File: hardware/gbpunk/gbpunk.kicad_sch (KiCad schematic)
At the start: 59 parts, among them J1 CART, J2 SWD_CONNECTOR, J4 SWD_CONNECTOR, P1 USB_C_CONNECTOR, SW7 RESET, SW9 USB_BOOT, U1 RP2040, U2 SN74LVC4245A, U3 W25Q128JVS, U4 NCP1117-3.3_SOT223, U5 SN74LVC4245A, U6 SN74LVC4245A, U7 SN74LVC4245A, Y1 12MHz

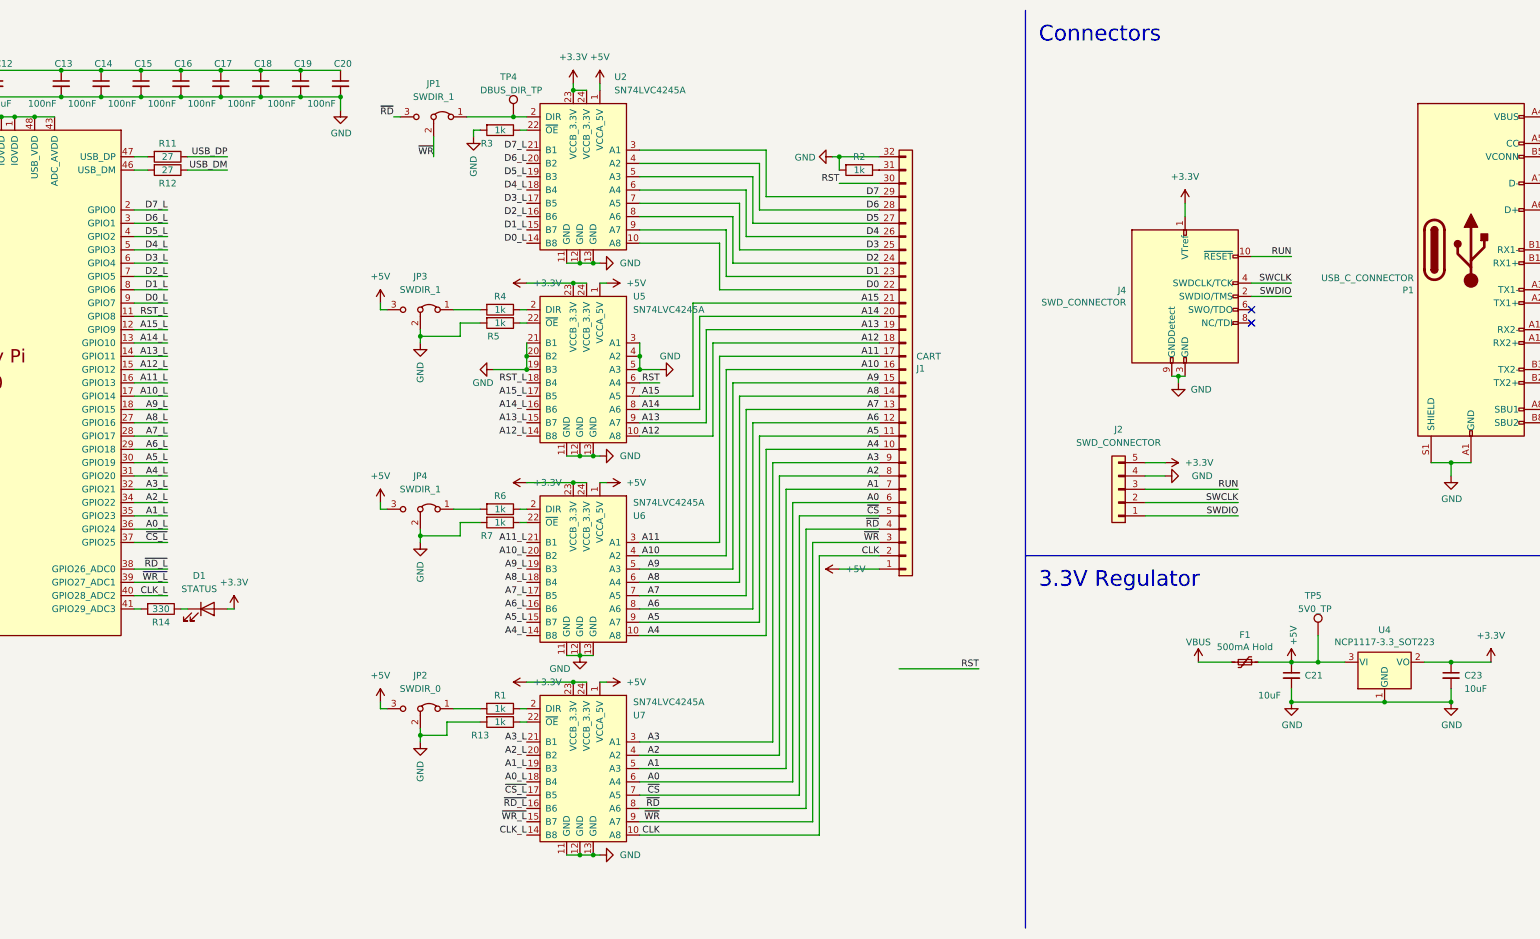
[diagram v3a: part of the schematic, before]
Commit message: added detection circuit and voltage switching for GBA/GB
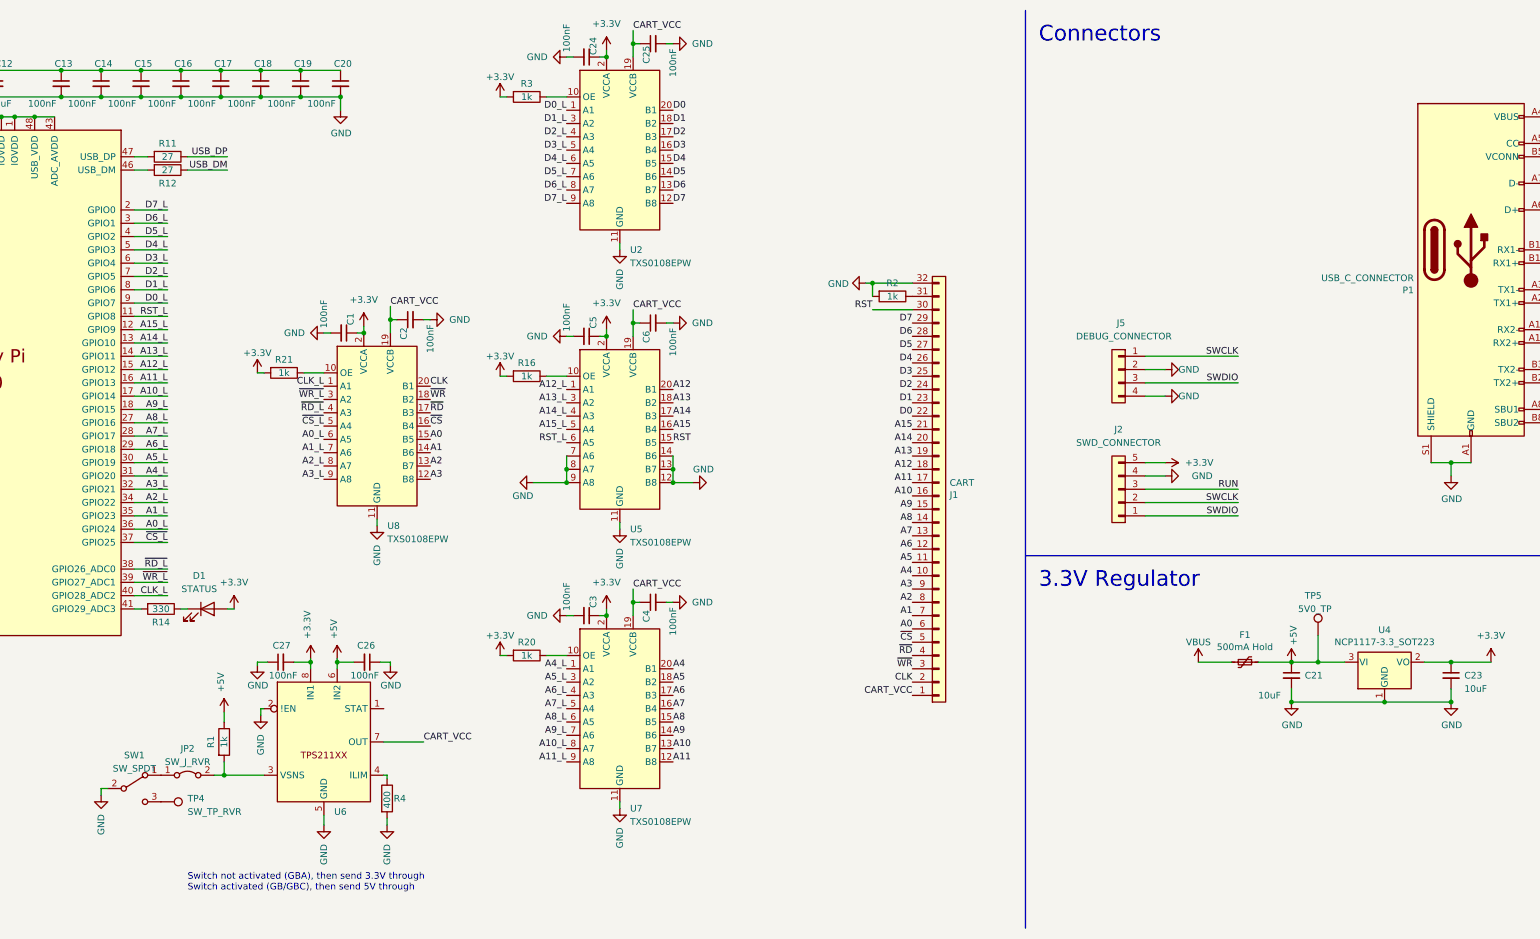
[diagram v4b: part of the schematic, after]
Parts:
- removed J4: SWD_CONNECTOR, Connector_PinHeader_1.27mm:PinHeader_2x05_P1.27mm_Vertical_SMD, symbol Connector:Conn_ARM_JTAG_SWD_10
- removed JP1, JP3, JP4: SWDIR_1, Jumper:SolderJumper-3_P1.3mm_Bridged12_RoundedPad1.0x1.5mm, symbol Jumper:Jumper_3_Bridged12
- removed JP2: SWDIR_0, Jumper:SolderJumper-3_P1.3mm_Bridged12_RoundedPad1.0x1.5mm, symbol Jumper:Jumper_3_Bridged12
- removed R13, R5, R6, R7: 1k, Resistor_SMD:R_0603_1608Metric_Pad0.98x0.95mm_HandSolder, symbol Device:R
- removed U2, U5, U6, U7: SN74LVC4245A, Package_SO:TSSOP-24_4.4x7.8mm_P0.65mm, symbol gbpunk:SN74LVC4245A
- added C1, C2, C24, C25, C26, C27, C3, C4, C5, C6: 100nF, Capacitor_SMD:C_0402_1005Metric_Pad0.74x0.62mm_HandSolder, symbol Device:C_Small
- added J5: DEBUG_CONNECTOR, Connector_JST:JST_GH_SM03B-GHS-TB_1x03-1MP_P1.25mm_Horizontal, symbol Connector_Generic:Conn_01x04
- added JP2: SW_J_RVR, symbol Jumper:Jumper_2_Bridged
- added R16, R20, R21: 1k, Resistor_SMD:R_0603_1608Metric_Pad0.98x0.95mm_HandSolder, symbol Device:R
- added SW1: SW_SPDT, symbol Switch:SW_SPDT
- added U2, U5, U7, U8: TXS0108EPW, Package_SO:TSSOP-20_4.4x6.5mm_P0.65mm, symbol Logic_LevelTranslator:TXS0108EPW
- added U6: ~, symbol gbpunk:TPS211XX
- R4: value 1k -> 400; footprint Resistor_SMD:R_0603_1608Metric_Pad0.98x0.95mm_HandSolder -> (none)
- TP4: value DBUS_DIR_TP -> SW_TP_RVR; footprint TestPoint:TestPoint_Pad_D1.0mm -> (none)
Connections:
- net +3.3V: now also R3.2, C1.1, C24.1, C27.2, C3.1, C5.1, R16.2, R20.2, R21.2, U2.2 (VCCA), U5.2 (VCCA), U6.8 (IN1), U7.2 (VCCA), U8.2 (VCCA)
- net +5V: now also R1.1, C26.2, U6.6 (IN2); no longer J1.1 (Pin_1)
- net A0: now also U8.15 (B5)
- net A0_L: now also U8.6 (A5)
- net A1: now also U8.14 (B6)
- net A10: now also U7.13 (B7)
- net A10_L: now also U7.8 (A7)
- net A11: now also U7.12 (B8)
- net A11_L: now also U7.9 (A8)
- net A12: now also U5.20 (B1)
- net A12_L: now also U5.1 (A1)
- net A13: now also U5.18 (B2)
- net A13_L: now also U5.3 (A2)
- net A14: now also U5.17 (B3)
- net A14_L: now also U5.4 (A3)
- net A15: now also U5.16 (B4)
- net A15_L: now also U5.5 (A4)
- net A1_L: now also U8.7 (A6)
- net A2: now also U8.13 (B7)
- net A2_L: now also U8.8 (A7)
- net A3: now also U8.12 (B8)
- net A3_L: now also U8.9 (A8)
- net A4: now also U7.20 (B1)
- net A4_L: now also U7.1 (A1)
- net A5: now also U7.18 (B2)
- net A5_L: now also U7.3 (A2)
- net A6: now also U7.17 (B3)
- net A6_L: now also U7.4 (A3)
- net A7: now also U7.16 (B4)
- net A7_L: now also U7.5 (A4)
- net A8: now also U7.15 (B5)
- net A8_L: now also U7.6 (A5)
- net A9: now also U7.14 (B6)
- net A9_L: now also U7.7 (A6)
- net CLK: now also U8.20 (B1)
- net CLK_L: now also U8.1 (A1)
- net D0: now also U2.20 (B1)
- net D0_L: now also U2.1 (A1)
- net D1: now also U2.18 (B2)
- net D1_L: now also U2.3 (A2)
- net D2: now also U2.17 (B3)
- net D2_L: now also U2.4 (A3)
- net D3: now also U2.16 (B4)
- net D3_L: now also U2.5 (A4)
- net D4: now also U2.15 (B5)
- net D4_L: now also U2.6 (A5)
- net D5: now also U2.14 (B6)
- net D5_L: now also U2.7 (A6)
- net D6: now also U2.13 (B7)
- net D6_L: now also U2.8 (A7)
- net D7: now also U2.12 (B8)
- net D7_L: now also U2.9 (A8)
- net GND: now also R4.2, C1.2, C2.2, C24.2, C25.2, C26.1, C27.1, C3.2, C4.2, C5.2, C6.2, J5.2 (Pin_2), J5.4 (Pin_4), SW1.2 (B), U2.11 (GND), U5.11 (GND), U5.12 (B8), U5.13 (B7), U5.14 (B6), U5.7 (A6), U5.8 (A7), U5.9 (A8), U6.2 (!EN), U6.5 (GND), U7.11 (GND), U8.11 (GND); no longer R3.2
- net RST: now also U5.15 (B5)
- net RST_L: now also U5.6 (A5)
- net SWCLK: now also J5.1 (Pin_1)
- net SWDIO: now also J5.3 (Pin_3)
- net ~{CS_L}: now also U8.5 (A4)
- net ~{CS}: now also U8.16 (B4)
- net ~{RD_L}: now also U8.4 (A3)
- net ~{RD}: now also U8.17 (B3)
- net ~{WR_L}: now also U8.3 (A2)
- net ~{WR}: now also U8.18 (B2)
- net at TP4.1: now also SW1.3 (C)
- net at R1.2: now also JP2.2 (B), U6.3 (VSNS)
- net at R3.1: now also U2.10 (OE)
- net at R4.1: now also U6.4 (ILIM)
- new net: R16.1, U5.10 (OE)
- new net: JP2.1 (A), SW1.1 (A)
- new net: R21.1, U8.10 (OE)
- new net: R20.1, U7.10 (OE)
- new net CART_VCC: C2.1, C25.1, C4.1, C6.1, J1.1 (Pin_1), U2.19 (VCCB), U5.19 (VCCB), U6.7 (OUT), U7.19 (VCCB), U8.19 (VCCB)
- no-connect marks 14 -> 12
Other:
- note added: "Switch not activated (GBA), then send 3.3V through Switch activated (GB/GBC), then send 5V through"
- moved on the sheet: J1, R2
